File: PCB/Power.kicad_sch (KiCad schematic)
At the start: 8 parts, among them U201 LM1117MP-3.3

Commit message: Created Bill of materials for the computer
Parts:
- TP201, TP202: now left out of the parts list
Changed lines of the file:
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@@
 		(unit 1)
 		(exclude_from_sim no)
-		(in_bom yes)
+		(in_bom no)
 		(on_board yes)
 		(dnp no)
@@
 		(unit 1)
 		(exclude_from_sim no)
-		(in_bom yes)
-		(on_board yes)
-		(dnp no)
+		(in_bom no)
+		(on_board yes)
+		(dnp no)

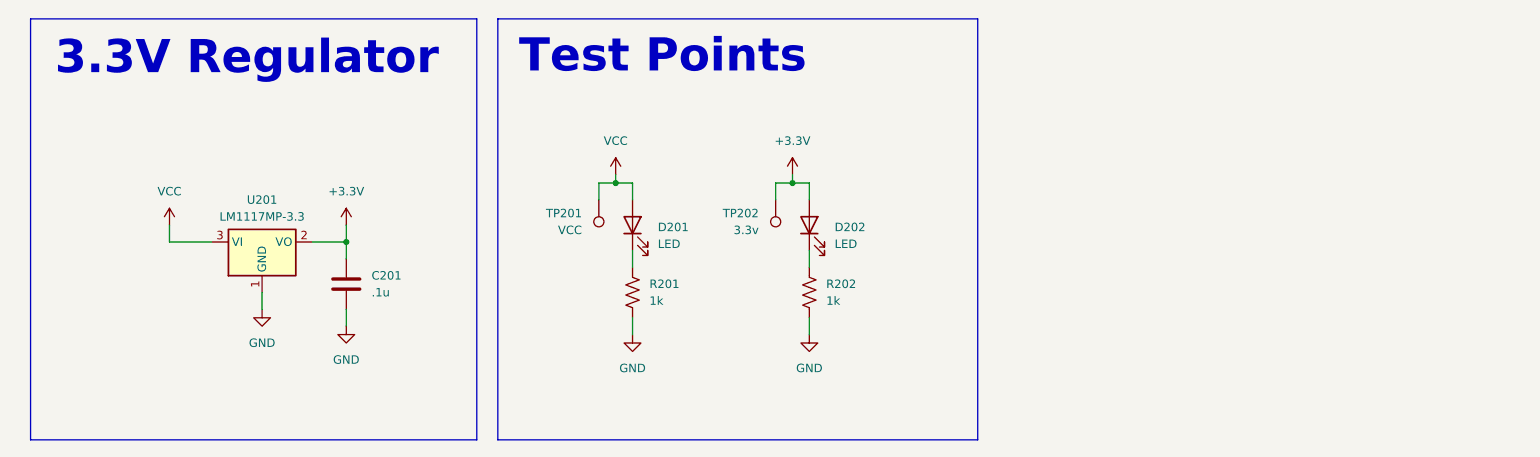
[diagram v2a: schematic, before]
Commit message: Switch from high side switch to low side switch for pyro channels
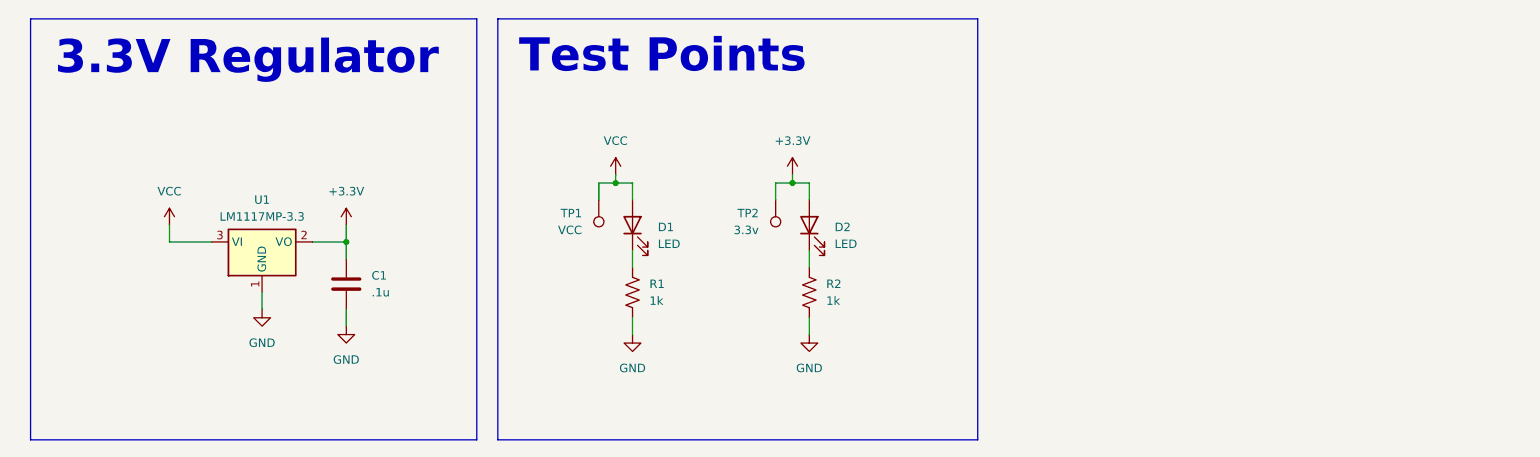
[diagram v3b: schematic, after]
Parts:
- renumbered C201 to C1, D201 to D1, D202 to D2, R201 to R1, R202 to R2, TP201 to TP1, TP202 to TP2, U201 to U1
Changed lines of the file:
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@@
 		(dnp no)
 		(fields_autoplaced yes)
-		(property "Reference" "#PWR0203"
+		(property "Reference" "#PWR03"
 			(at 36.83 50.8 0)
 			(effects
@@
 			(project "Flight Computer"
 				(path "/4254ccd1-49f4-4fe6-9bf7-ccb200d73af4/ce25203d-742b-46bf-b676-aa9cb5879333"
-					(reference "#PWR0203")
+					(reference "#PWR03")
 					(unit 1)
 				)
@@
 		(dnp no)
 		(fields_autoplaced yes)
-		(property "Reference" "#PWR0205"
+		(property "Reference" "#PWR05"
 			(at 50.8 66.04 0)
 			(effects
@@
 			(project "Flight Computer"
 				(path "/4254ccd1-49f4-4fe6-9bf7-ccb200d73af4/ce25203d-742b-46bf-b676-aa9cb5879333"
-					(reference "#PWR0205")
+					(reference "#PWR05")
 					(unit 1)
 				)
@@
 		(dnp no)
 		(fields_autoplaced yes)
-		(property "Reference" "#PWR0206"
+		(property "Reference" "#PWR06"
 			(at 63.5 68.58 0)
 			(effects
@@
 			(project "Flight Computer"
 				(path "/4254ccd1-49f4-4fe6-9bf7-ccb200d73af4/ce25203d-742b-46bf-b676-aa9cb5879333"
-					(reference "#PWR0206")
+					(reference "#PWR06")
 					(unit 1)
 				)
@@
 		(dnp no)
 		(fields_autoplaced yes)
-		(property "Reference" "C201"
+		(property "Reference" "C1"
 			(at 67.31 54.6099 0)
 			(effects
@@
 			(project ""
 				(path "/4254ccd1-49f4-4fe6-9bf7-ccb200d73af4/ce25203d-742b-46bf-b676-aa9cb5879333"
-					(reference "C201")
+					(reference "C1")
 					(unit 1)
 				)
@@
 		(dnp no)
 		(fields_autoplaced yes)
-		(property "Reference" "#PWR0208"
+		(property "Reference" "#PWR08"
 			(at 133.35 69.85 0)
 			(effects
@@
 			(project "Flight Computer"
 				(path "/4254ccd1-49f4-4fe6-9bf7-ccb200d73af4/ce25203d-742b-46bf-b676-aa9cb5879333"
-					(reference "#PWR0208")
+					(reference "#PWR08")
 					(unit 1)
 				)
@@
 		(dnp no)
 		(fields_autoplaced yes)
-		(property "Reference" "#PWR0204"
+		(property "Reference" "#PWR04"
 			(at 63.5 50.8 0)
 			(effects
@@
 			(project ""
 				(path "/4254ccd1-49f4-4fe6-9bf7-ccb200d73af4/ce25203d-742b-46bf-b676-aa9cb5879333"
-					(reference "#PWR0204")
+					(reference "#PWR04")
 					(unit 1)
 				)
@@
 		(dnp no)
 		(fields_autoplaced yes)
-		(property "Reference" "#PWR0202"
+		(property "Reference" "#PWR02"
 			(at 130.81 43.18 0)
 			(effects
@@
 			(project ""
 				(path "/4254ccd1-49f4-4fe6-9bf7-ccb200d73af4/ce25203d-742b-46bf-b676-aa9cb5879333"
-					(reference "#PWR0202")
+					(reference "#PWR02")
 					(unit 1)
 				)
@@
 		(dnp no)
 		(fields_autoplaced yes)
-		(property "Reference" "R202"
+		(property "Reference" "R2"
 			(at 135.89 55.8799 0)
 			(effects
@@
 			(project "Flight Computer"
 				(path "/4254ccd1-49f4-4fe6-9bf7-ccb200d73af4/ce25203d-742b-46bf-b676-aa9cb5879333"
-					(reference "R202")
+					(reference "R2")
 					(unit 1)
 				)
@@
 		(dnp no)
 		(fields_autoplaced yes)
-		(property "Reference" "U201"
+		(property "Reference" "U1"
 			(at 50.8 43.18 0)
 			(effects
@@
 			(project ""
 				(path "/4254ccd1-49f4-4fe6-9bf7-ccb200d73af4/ce25203d-742b-46bf-b676-aa9cb5879333"
-					(reference "U201")
+					(reference "U1")
 					(unit 1)
 				)
@@
 		(on_board yes)
 		(dnp no)
-		(property "Reference" "TP201"
+		(property "Reference" "TP1"
 			(at 99.06 45.2119 0)
 			(effects
@@
 			(project ""
 				(path "/4254ccd1-49f4-4fe6-9bf7-ccb200d73af4/ce25203d-742b-46bf-b676-aa9cb5879333"
-					(reference "TP201")
+					(reference "TP1")
 					(unit 1)
 				)
@@
 		(dnp no)
 		(fields_autoplaced yes)
-		(property "Reference" "#PWR0201"
+		(property "Reference" "#PWR01"
 			(at 104.14 43.18 0)
 			(effects
@@
 			(project ""
 				(path "/4254ccd1-49f4-4fe6-9bf7-ccb200d73af4/ce25203d-742b-46bf-b676-aa9cb5879333"
-					(reference "#PWR0201")
+					(reference "#PWR01")
 					(unit 1)
 				)
@@
 		(dnp no)
 		(fields_autoplaced yes)
-		(property "Reference" "#PWR0207"
+		(property "Reference" "#PWR07"
 			(at 106.68 69.85 0)
 			(effects
@@
 			(project ""
 				(path "/4254ccd1-49f4-4fe6-9bf7-ccb200d73af4/ce25203d-742b-46bf-b676-aa9cb5879333"
-					(reference "#PWR0207")
+					(reference "#PWR07")
 					(unit 1)
 				)
@@
 		(dnp no)
 		(fields_autoplaced yes)
-		(property "Reference" "R201"
+		(property "Reference" "R1"
 			(at 109.22 55.8799 0)
 			(effects
@@
 			(project "Flight Computer"
 				(path "/4254ccd1-49f4-4fe6-9bf7-ccb200d73af4/ce25203d-742b-46bf-b676-aa9cb5879333"
-					(reference "R201")
+					(reference "R1")
 					(unit 1)
 				)
@@
 		(on_board yes)
 		(dnp no)
-		(property "Reference" "TP202"
+		(property "Reference" "TP2"
 			(at 125.73 45.2119 0)
 			(effects
@@
 			(project "Flight Computer"
 				(path "/4254ccd1-49f4-4fe6-9bf7-ccb200d73af4/ce25203d-742b-46bf-b676-aa9cb5879333"
-					(reference "TP202")
+					(reference "TP2")
 					(unit 1)
 				)
@@
 		(dnp no)
 		(fields_autoplaced yes)
-		(property "Reference" "D201"
+		(property "Reference" "D1"
 			(at 110.49 47.3074 90)
 			(effects
@@
 			(project ""
 				(path "/4254ccd1-49f4-4fe6-9bf7-ccb200d73af4/ce25203d-742b-46bf-b676-aa9cb5879333"
-					(reference "D201")
+					(reference "D1")
 					(unit 1)
 				)
@@
 		(dnp no)
 		(fields_autoplaced yes)
-		(property "Reference" "D202"
+		(property "Reference" "D2"
 			(at 137.16 47.3074 90)
 			(effects
@@
 			(project "Flight Computer"
 				(path "/4254ccd1-49f4-4fe6-9bf7-ccb200d73af4/ce25203d-742b-46bf-b676-aa9cb5879333"
-					(reference "D202")
-					(unit 1)
-				)
+					(reference "D2")
+					(unit 1)
+				)

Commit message: Fixed component annotation Updated BOM to reflect the pyro channel changes Updates Production files
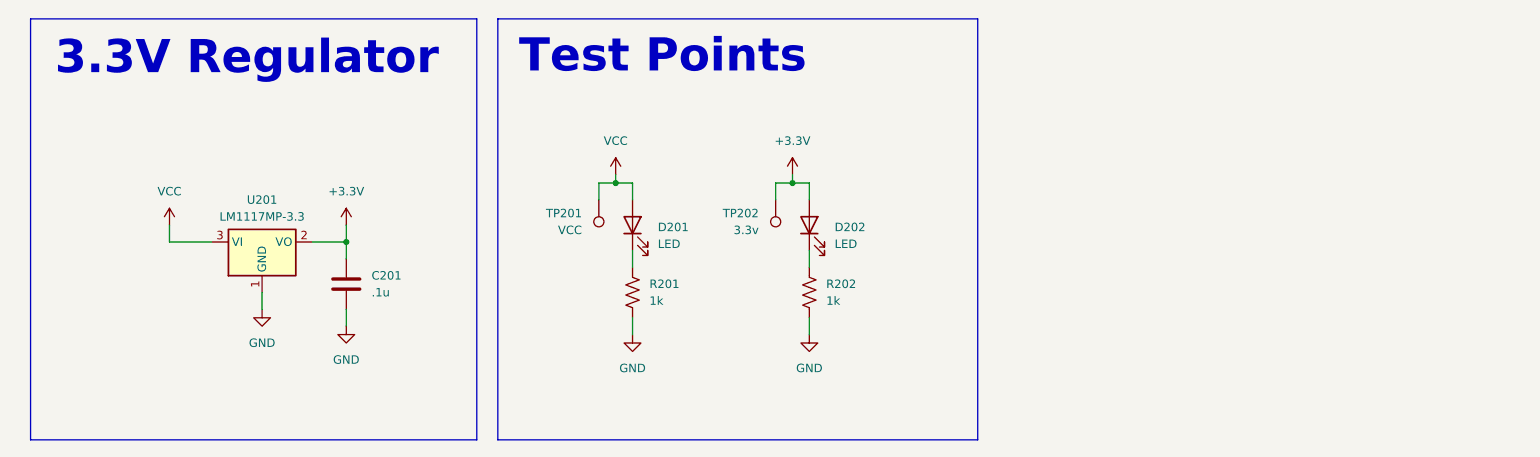
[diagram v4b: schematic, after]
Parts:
- renumbered C1 to C201, D1 to D201, D2 to D202, R1 to R201, R2 to R202, TP1 to TP201, TP2 to TP202, U1 to U201
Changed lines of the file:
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@@
 		(dnp no)
 		(fields_autoplaced yes)
-		(property "Reference" "#PWR03"
+		(property "Reference" "#PWR0203"
 			(at 36.83 50.8 0)
 			(effects
@@
 			(project "Flight Computer"
 				(path "/4254ccd1-49f4-4fe6-9bf7-ccb200d73af4/ce25203d-742b-46bf-b676-aa9cb5879333"
-					(reference "#PWR03")
+					(reference "#PWR0203")
 					(unit 1)
 				)
@@
 		(dnp no)
 		(fields_autoplaced yes)
-		(property "Reference" "#PWR05"
+		(property "Reference" "#PWR0205"
 			(at 50.8 66.04 0)
 			(effects
@@
 			(project "Flight Computer"
 				(path "/4254ccd1-49f4-4fe6-9bf7-ccb200d73af4/ce25203d-742b-46bf-b676-aa9cb5879333"
-					(reference "#PWR05")
+					(reference "#PWR0205")
 					(unit 1)
 				)
@@
 		(dnp no)
 		(fields_autoplaced yes)
-		(property "Reference" "#PWR06"
+		(property "Reference" "#PWR0206"
 			(at 63.5 68.58 0)
 			(effects
@@
 			(project "Flight Computer"
 				(path "/4254ccd1-49f4-4fe6-9bf7-ccb200d73af4/ce25203d-742b-46bf-b676-aa9cb5879333"
-					(reference "#PWR06")
+					(reference "#PWR0206")
 					(unit 1)
 				)
@@
 		(dnp no)
 		(fields_autoplaced yes)
-		(property "Reference" "C1"
+		(property "Reference" "C201"
 			(at 67.31 54.6099 0)
 			(effects
@@
 			(project ""
 				(path "/4254ccd1-49f4-4fe6-9bf7-ccb200d73af4/ce25203d-742b-46bf-b676-aa9cb5879333"
-					(reference "C1")
+					(reference "C201")
 					(unit 1)
 				)
@@
 		(dnp no)
 		(fields_autoplaced yes)
-		(property "Reference" "#PWR08"
+		(property "Reference" "#PWR0208"
 			(at 133.35 69.85 0)
 			(effects
@@
 			(project "Flight Computer"
 				(path "/4254ccd1-49f4-4fe6-9bf7-ccb200d73af4/ce25203d-742b-46bf-b676-aa9cb5879333"
-					(reference "#PWR08")
+					(reference "#PWR0208")
 					(unit 1)
 				)
@@
 		(dnp no)
 		(fields_autoplaced yes)
-		(property "Reference" "#PWR04"
+		(property "Reference" "#PWR0204"
 			(at 63.5 50.8 0)
 			(effects
@@
 			(project ""
 				(path "/4254ccd1-49f4-4fe6-9bf7-ccb200d73af4/ce25203d-742b-46bf-b676-aa9cb5879333"
-					(reference "#PWR04")
+					(reference "#PWR0204")
 					(unit 1)
 				)
@@
 		(dnp no)
 		(fields_autoplaced yes)
-		(property "Reference" "#PWR02"
+		(property "Reference" "#PWR0202"
 			(at 130.81 43.18 0)
 			(effects
@@
 			(project ""
 				(path "/4254ccd1-49f4-4fe6-9bf7-ccb200d73af4/ce25203d-742b-46bf-b676-aa9cb5879333"
-					(reference "#PWR02")
+					(reference "#PWR0202")
 					(unit 1)
 				)
@@
 		(dnp no)
 		(fields_autoplaced yes)
-		(property "Reference" "R2"
+		(property "Reference" "R202"
 			(at 135.89 55.8799 0)
 			(effects
@@
 			(project "Flight Computer"
 				(path "/4254ccd1-49f4-4fe6-9bf7-ccb200d73af4/ce25203d-742b-46bf-b676-aa9cb5879333"
-					(reference "R2")
+					(reference "R202")
 					(unit 1)
 				)
@@
 		(dnp no)
 		(fields_autoplaced yes)
-		(property "Reference" "U1"
+		(property "Reference" "U201"
 			(at 50.8 43.18 0)
 			(effects
@@
 			(project ""
 				(path "/4254ccd1-49f4-4fe6-9bf7-ccb200d73af4/ce25203d-742b-46bf-b676-aa9cb5879333"
-					(reference "U1")
+					(reference "U201")
 					(unit 1)
 				)
@@
 		(on_board yes)
 		(dnp no)
-		(property "Reference" "TP1"
+		(property "Reference" "TP201"
 			(at 99.06 45.2119 0)
 			(effects
@@
 			(project ""
 				(path "/4254ccd1-49f4-4fe6-9bf7-ccb200d73af4/ce25203d-742b-46bf-b676-aa9cb5879333"
-					(reference "TP1")
+					(reference "TP201")
 					(unit 1)
 				)
@@
 		(dnp no)
 		(fields_autoplaced yes)
-		(property "Reference" "#PWR01"
+		(property "Reference" "#PWR0201"
 			(at 104.14 43.18 0)
 			(effects
@@
 			(project ""
 				(path "/4254ccd1-49f4-4fe6-9bf7-ccb200d73af4/ce25203d-742b-46bf-b676-aa9cb5879333"
-					(reference "#PWR01")
+					(reference "#PWR0201")
 					(unit 1)
 				)
@@
 		(dnp no)
 		(fields_autoplaced yes)
-		(property "Reference" "#PWR07"
+		(property "Reference" "#PWR0207"
 			(at 106.68 69.85 0)
 			(effects
@@
 			(project ""
 				(path "/4254ccd1-49f4-4fe6-9bf7-ccb200d73af4/ce25203d-742b-46bf-b676-aa9cb5879333"
-					(reference "#PWR07")
+					(reference "#PWR0207")
 					(unit 1)
 				)
@@
 		(dnp no)
 		(fields_autoplaced yes)
-		(property "Reference" "R1"
+		(property "Reference" "R201"
 			(at 109.22 55.8799 0)
 			(effects
@@
 			(project "Flight Computer"
 				(path "/4254ccd1-49f4-4fe6-9bf7-ccb200d73af4/ce25203d-742b-46bf-b676-aa9cb5879333"
-					(reference "R1")
+					(reference "R201")
 					(unit 1)
 				)
@@
 		(on_board yes)
 		(dnp no)
-		(property "Reference" "TP2"
+		(property "Reference" "TP202"
 			(at 125.73 45.2119 0)
 			(effects
@@
 			(project "Flight Computer"
 				(path "/4254ccd1-49f4-4fe6-9bf7-ccb200d73af4/ce25203d-742b-46bf-b676-aa9cb5879333"
-					(reference "TP2")
+					(reference "TP202")
 					(unit 1)
 				)
@@
 		(dnp no)
 		(fields_autoplaced yes)
-		(property "Reference" "D1"
+		(property "Reference" "D201"
 			(at 110.49 47.3074 90)
 			(effects
@@
 			(project ""
 				(path "/4254ccd1-49f4-4fe6-9bf7-ccb200d73af4/ce25203d-742b-46bf-b676-aa9cb5879333"
-					(reference "D1")
+					(reference "D201")
 					(unit 1)
 				)
@@
 		(dnp no)
 		(fields_autoplaced yes)
-		(property "Reference" "D2"
+		(property "Reference" "D202"
 			(at 137.16 47.3074 90)
 			(effects
@@
 			(project "Flight Computer"
 				(path "/4254ccd1-49f4-4fe6-9bf7-ccb200d73af4/ce25203d-742b-46bf-b676-aa9cb5879333"
-					(reference "D2")
-					(unit 1)
-				)
+					(reference "D202")
+					(unit 1)
+				)

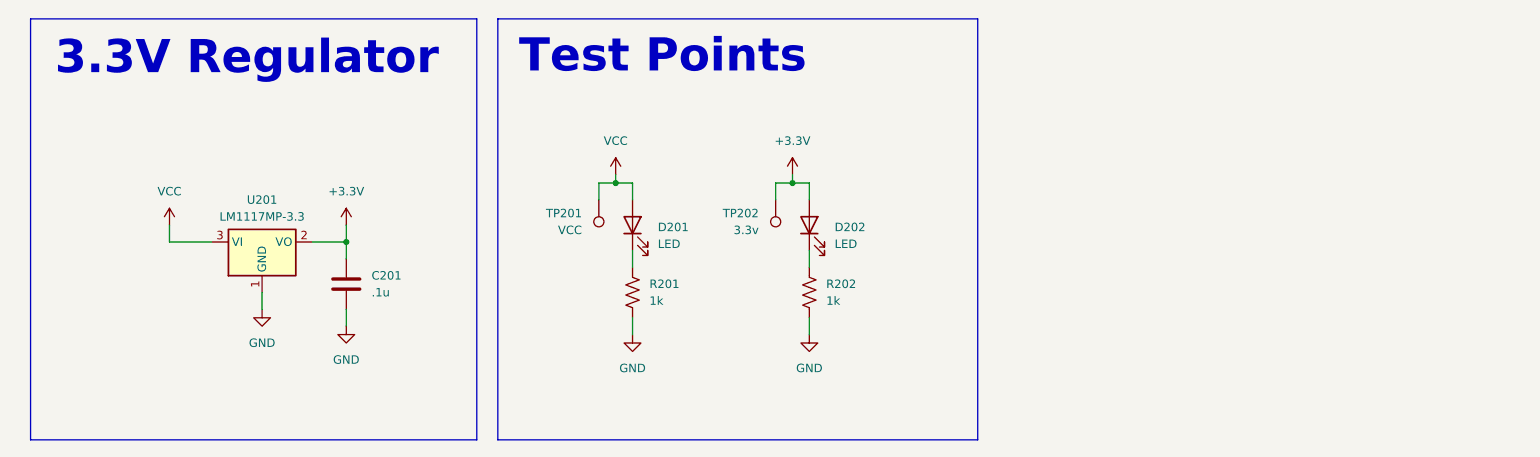
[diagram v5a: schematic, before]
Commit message: Replaced the radio in the schematic
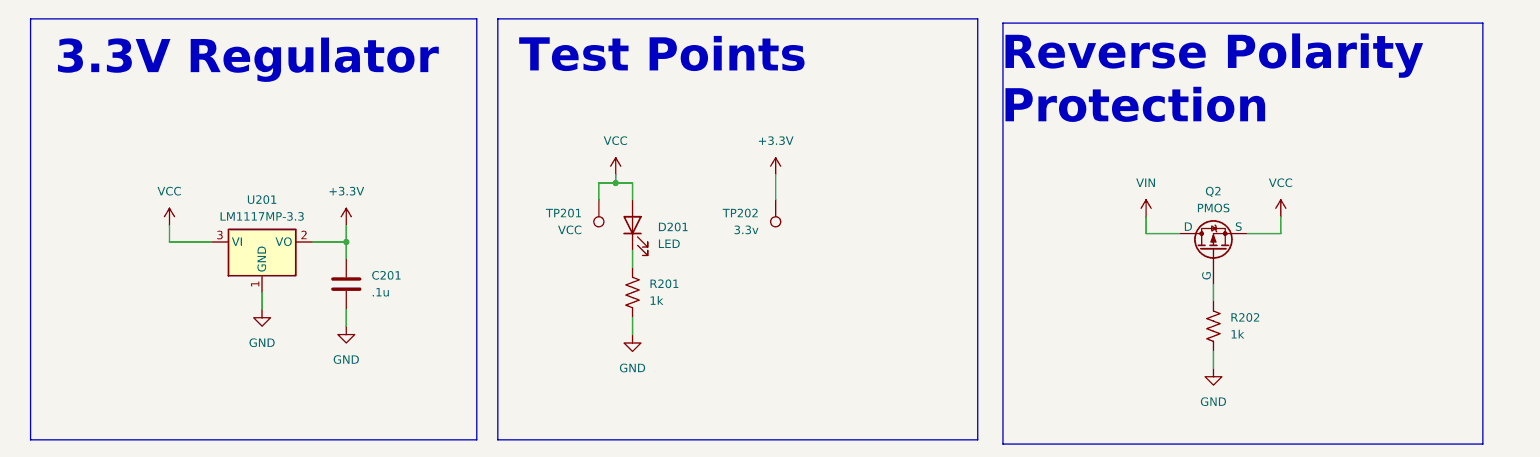
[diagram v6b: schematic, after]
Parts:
- removed D202: LED, LED_SMD:LED_0603_1608Metric_Pad1.05x0.95mm_HandSolder, symbol Device:LED
- added Q2: PMOS, symbol Simulation_SPICE:PMOS
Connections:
- net VCC: now also Q2.3 (S)
- net at R202.2: now also Q2.2 (G)
- new net VIN: Q2.1 (D)
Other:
- note added: "Reverse Polarity Protection"
